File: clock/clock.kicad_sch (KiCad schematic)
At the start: 3 parts, among them P101 CONN_01X03, P102 CONN_FAN_PWM, P103 XG4A-1631

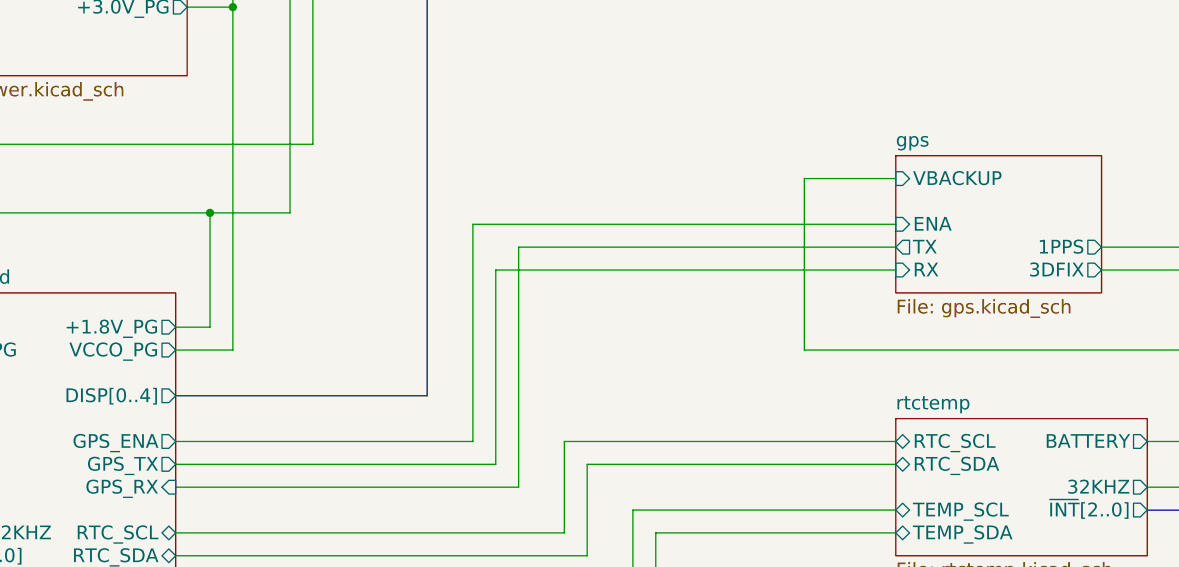
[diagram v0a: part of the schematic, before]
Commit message: Make some net names consistent with hierarchy names. Clean up some silkscreen DRCs.
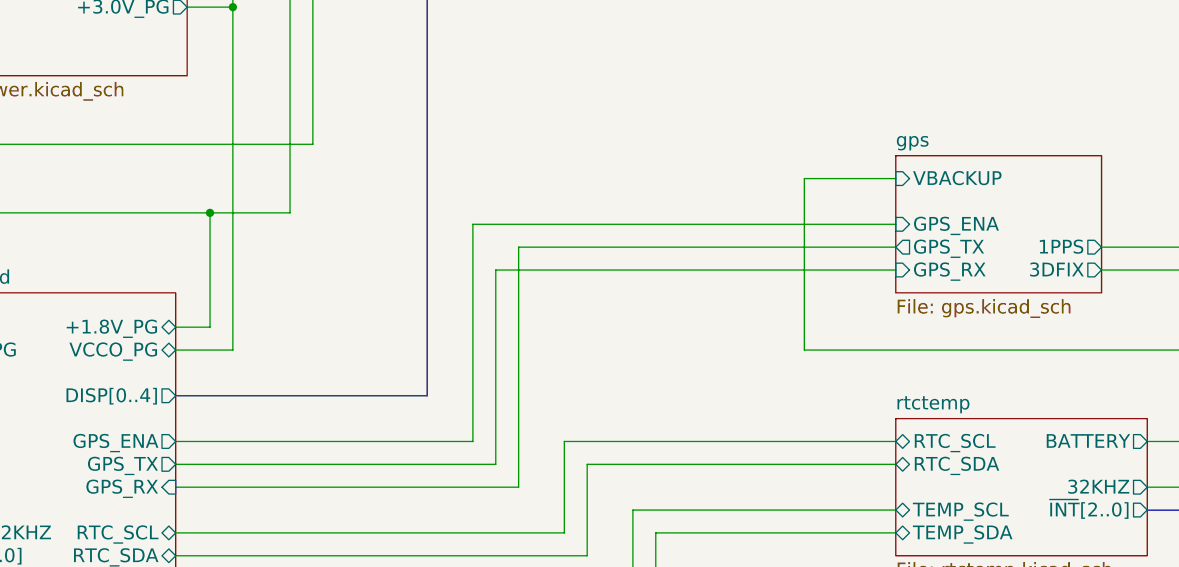
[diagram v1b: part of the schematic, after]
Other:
- sheet gps ports: added GPS_ENA, GPS_RX, GPS_TX; removed ENA, RX, TX
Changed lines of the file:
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@@
 			)
 		)
-		(pin "TX" output
+		(pin "GPS_TX" output
 			(at 168.91 72.39 180)
 			(effects
@@
 			)
 		)
-		(pin "RX" input
+		(pin "GPS_RX" input
 			(at 168.91 74.93 180)
 			(effects
@@
 			)
 		)
-		(pin "ENA" input
+		(pin "GPS_ENA" input
 			(at 168.91 69.85 180)
 			(effects
@@
 			)
 		)
-		(pin "+1.8V_PG" output
+		(pin "+1.8V_PG" bidirectional
 			(at 88.9 81.28 0)
 			(effects
@@
 			)
 		)
-		(pin "VCCO_PG" output
+		(pin "VCCO_PG" bidirectional
 			(at 88.9 83.82 0)
 			(effects

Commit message: Bump version string of clock to v1.2.0.
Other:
- title: Clock -> Clock, NTP server w/ GPS disciplined OCXO
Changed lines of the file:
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@@
 	(paper "A4")
 	(title_block
-		(title "Clock")
-		(date "2019-12-09")
-		(rev "1.1.2")
+		(title "Clock, NTP server w/ GPS disciplined OCXO")
+		(date "2025-01-27")
+		(rev "v1.2.0")
 	)
 	(junction
